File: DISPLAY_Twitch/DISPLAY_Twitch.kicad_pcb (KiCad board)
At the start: 4 copper layers, 60 x 60 mm, 101 parts, among them J1 Conn_01x06_Pin, J2 Conn_01x06_Pin, Q1 Q_PNP_BEC, Q10 Q_PNP_BEC, Q11 Q_PNP_BEC, Q12 Q_NPN_BEC, Q13 Q_PNP_BEC, Q14 Q_NPN_BEC, Q15 Q_PNP_BEC, Q16 Q_PNP_BEC, Q17 Q_NPN_BEC, Q18 Q_PNP_BEC, Q2 Q_PNP_BEC, Q3 Q_PNP_BEC, Q4 Q_PMOS_GSD, Q5 Q_PMOS_GSD, Q6 Q_PNP_BEC, Q7 Q_PNP_BEC, Q8 Q_PMOS_GSD, Q9 Q_PNP_BEC, SW1 MSK12C02, SW2 MSK12C02, SW3 MSK12C02, U1 3VM11201-D730-7H, U2 3VM11201-D730-7H, U3 3VM11201-D730-7H, U4 3VM11201-D730-7H, U5 FSW3820YQFN32G/TR, U6 FSW3820YQFN32G/TR, U7 FSW3820YQFN32G/TR, U8 FSW3820YQFN32G/TR

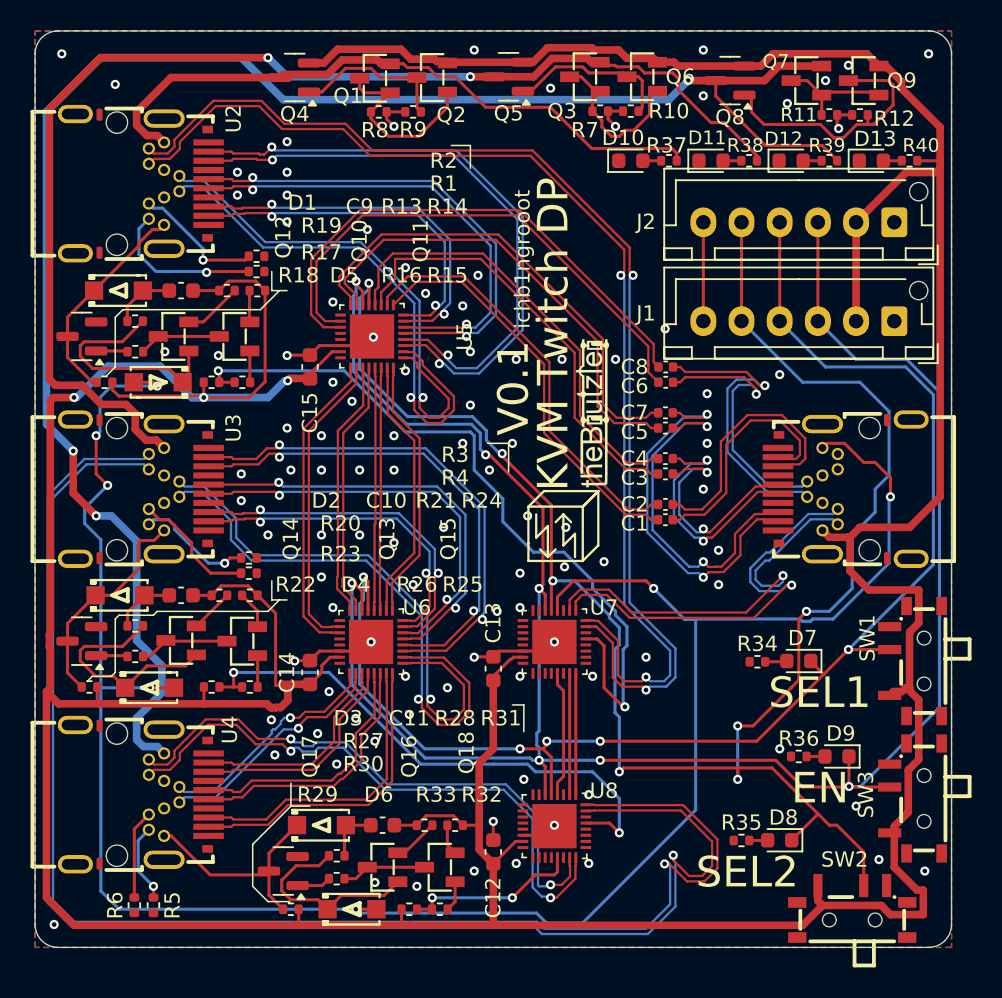
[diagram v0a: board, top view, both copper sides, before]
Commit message: add nev versions. (usb c and displayport working)
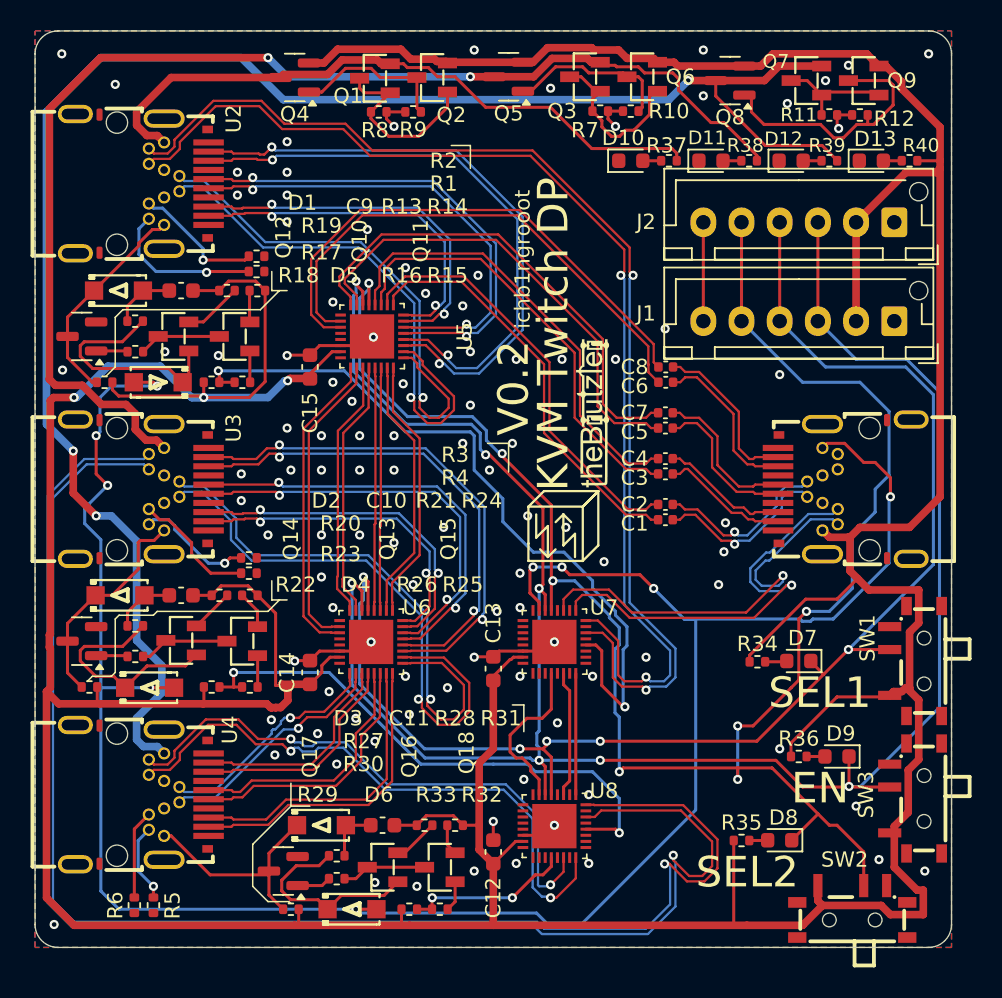
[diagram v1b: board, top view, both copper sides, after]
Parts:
- C1, C2, C3, C4, C5, C6, C7, C8: value C -> 100n
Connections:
- C1 pad 1: /L0C+ -> /L3C-
- C1 pad 2: /L0+ -> /L3-
- C2 pad 1: /L0C- -> /L3C+
- C2 pad 2: /L0- -> /L3+
- C3 pad 1: /L1C+ -> /L2C-
- C3 pad 2: /L1+ -> /L2-
- C4 pad 1: /L1C- -> /L2C+
- C4 pad 2: /L1- -> /L2+
- C5 pad 1: /L2C+ -> /L1C-
- C5 pad 2: /L2+ -> /L1-
- C6 pad 1: /L3C+ -> /L0C-
- C6 pad 2: /L3+ -> /L0-
- C7 pad 1: /L2C- -> /L1C+
- C7 pad 2: /L2- -> /L1+
- C8 pad 1: /L3C- -> /L0C+
- C8 pad 2: /L3- -> /L0+
- R34 pad 1: GND -> +3V3
- R35 pad 1: GND -> +3V3
- R36 pad 1: GND -> +3V3
- U3 pad 18: /AXB- -> unconnected-(U3-AUX_CH--Pad18)
- U5 pad 1: /L0C+ -> /L3C-
- U5 pad 10: /L3C+ -> /L0C-
- U5 pad 11: /L3C- -> /L0C+
- U5 pad 2: /L0C- -> /L3C+
- U5 pad 3: /L1C+ -> /L2C-
- U5 pad 4: /L1C- -> /L2C+
- U5 pad 7: /L2C+ -> /L1C-
- U5 pad 8: /L2C- -> /L1C+
- U7 pad 2: /AX- -> unconnected-(U7-D0--Pad2)
- U7 pad 20: unconnected-(U7-D2+B-Pad20) -> Net-(U7-D2+B)
- U7 pad 21: Net-(U7-D1-B) -> unconnected-(U7-D1-B-Pad21)
- U7 pad 22: unconnected-(U7-D1+B-Pad22) -> Net-(U7-D1+B)
- U7 pad 23: Net-(U7-D0-B) -> unconnected-(U7-D0-B-Pad23)
- U7 pad 28: unconnected-(U7-D2+A-Pad28) -> /HPD_IN_A
- U7 pad 29: /HPD_IN_A -> unconnected-(U7-D1-A-Pad29)
- U7 pad 3: unconnected-(U7-D1+-Pad3) -> /AX-
- U7 pad 30: unconnected-(U7-D1+A-Pad30) -> /AXA-
- U7 pad 31: /AXA- -> unconnected-(U7-D0-A-Pad31)
- U7 pad 4: /HPD_SELV_TRIP/HPD_IN -> unconnected-(U7-D1--Pad4)
- U7 pad 7: unconnected-(U7-D2+-Pad7) -> /HPD_SELV_TRIP/HPD_IN
- U8 pad 2: Net-(U7-D0-B) -> unconnected-(U8-D0--Pad2)
- U8 pad 20: unconnected-(U8-D2+B-Pad20) -> /HPD_IN_C
- U8 pad 21: /HPD_IN_C -> unconnected-(U8-D1-B-Pad21)
- U8 pad 22: unconnected-(U8-D1+B-Pad22) -> /AXC-
- U8 pad 23: /AXC- -> unconnected-(U8-D0-B-Pad23)
- U8 pad 28: unconnected-(U8-D2+A-Pad28) -> /HPD_IN_B
- U8 pad 29: /HPD_IN_B -> unconnected-(U8-D1-A-Pad29)
- U8 pad 3: unconnected-(U8-D1+-Pad3) -> Net-(U7-D1+B)
- U8 pad 30: unconnected-(U8-D1+A-Pad30) -> /AXB-
- U8 pad 31: /AXB- -> unconnected-(U8-D0-A-Pad31)
- U8 pad 4: Net-(U7-D1-B) -> unconnected-(U8-D1--Pad4)
- U8 pad 7: unconnected-(U8-D2+-Pad7) -> Net-(U7-D2+B)
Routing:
- net +3V3: track 334.5 -> 359.1 mm
- net /L2-: track 24.8 -> 8.44 mm, vias 2 -> 0
- net /L2+: track 23.6 -> 8.44 mm, vias 2 -> 0
- net Net-(U7-D2+B): track 0.00 -> 10.7 mm
- net /L3-: track 20.0 -> 11.7 mm
- net Net-(U7-D1-B): track 8.27 -> 0.00 mm
- net Net-(U7-D1+B): track 0.00 -> 8.27 mm
- net Net-(U7-D0-B): track 7.94 -> 0.00 mm
- net /L0C+: track 27.0 -> 34.9 mm
- net /L3C-: track 34.9 -> 27.4 mm
- net /L3+: track 18.2 -> 11.7 mm
- net /L0C-: track 27.9 -> 34.3 mm
- net /L1-: track 16.5 -> 10.1 mm, vias 2 -> 0
- net /L0-: track 17.2 -> 10.8 mm
- net /L3C+: track 34.3 -> 28.0 mm
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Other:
- board text added: "V0.2"
- board text removed: "V0.1"
